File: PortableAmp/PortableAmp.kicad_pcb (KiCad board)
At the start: 2 copper layers, 5 x 45 mm, 19 parts, among them J1 Conn_01x04_Male, J2 Speaker, Q1 MPF102, U1 LM386

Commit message: Minor changes
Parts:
- moved J2 29.8 mm to (144.8, 79.0), turned to 270 degrees
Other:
- board text added: "+"
- board text added: "-"
- board text added: "Speaker"
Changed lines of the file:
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@@
   (general
     (thickness 1.6)
-    (drawings 7)
+    (drawings 10)
     (tracks 0)
     (zones 0)
@@
   )
   (module Connector_PinSocket_2.54mm:PinSocket_1x02_P2.54mm_Vertical (layer F.Cu)
-    (at 149.459001 49.577001)
+    (at 144.78 79 270)
     (descr "Through hole straight socket strip, 1x02, 2.54mm pitch, single row (from Kicad 4.0.7), script generated")
     (tags "Through hole socket strip THT 1x02 2.54mm single row")
-    (fp_text reference J2 (at 0 -2.77) (layer F.SilkS)
-      (effects (font (size 1 1) (thickness 0.15)))
-    )
-    (fp_text value Speaker (at 0 5.31) (layer F.Fab)
+    (fp_text reference J2 (at 0 -2.77 180) (layer F.SilkS)
+      (effects (font (size 1 1) (thickness 0.15)))
+    )
+    (fp_text value Speaker (at 0 5.31 90) (layer F.Fab)
       (effects (font (size 1 1) (thickness 0.15)))
     )
@@
     (fp_line (start 1.75 4.3) (end -1.8 4.3) (layer F.CrtYd) (width 0.05))
     (fp_line (start -1.8 4.3) (end -1.8 -1.8) (layer F.CrtYd) (width 0.05))
-    (fp_text user %R (at 0 1.27 90) (layer F.Fab)
-      (effects (font (size 1 1) (thickness 0.15)))
-    )
-    (pad 1 thru_hole rect (at 0 0) (size 1.7 1.7) (drill 1) (layers *.Cu *.Mask)
-      (net 2 GND))
-    (pad 2 thru_hole oval (at 0 2.54) (size 1.7 1.7) (drill 1) (layers *.Cu *.Mask)
+    (fp_text user %R (at 0 1.27) (layer F.Fab)
+      (effects (font (size 1 1) (thickness 0.15)))
+    )
+    (pad 1 thru_hole rect (at 0 0 270) (size 1.7 1.7) (drill 1) (layers *.Cu *.Mask)
+      (net 2 GND))
+    (pad 2 thru_hole oval (at 0 2.54 270) (size 1.7 1.7) (drill 1) (layers *.Cu *.Mask)
       (net 7 "Net-(C5-Pad2)"))
     (model ${KISYS3DMOD}/Connector_PinSocket_2.54mm.3dshapes/PinSocket_1x02_P2.54mm_Vertical.wrl
@@
       (net 2 GND))
   )
+  (gr_text - (at 144.78 76.23) (layer F.SilkS)
+    (effects (font (size 1.5 1.5) (thickness 0.3)))
+  )
+  (gr_text + (at 142.24 76.23) (layer F.SilkS)
+    (effects (font (size 1.5 1.5) (thickness 0.3)))
+  )
+  (gr_text Speaker (at 143.51 81.77) (layer F.SilkS)
+    (effects (font (size 1 1) (thickness 0.15)))
+  )
   (gr_text GND (at 155.194 93.98) (layer F.SilkS)

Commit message: Finalized board and exported gerbers
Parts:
- moved D1 70.5 mm to (142.2, 107.2)
- moved C4 52.6 mm to (113.3, 94.5), turned to 180 degrees
- moved R2 50.7 mm to (103.6, 98.6)
- moved R1 50.1 mm to (113.8, 102.1), turned to 180 degrees
- moved R3 49.6 mm to (113.8, 105.7), turned to 180 degrees
- moved Q1 43.4 mm to (133.6, 104.6), turned to 180 degrees
- moved C3 43.0 mm to (145.8, 99.8), turned to 180 degrees
- moved H2 42.1 mm to (103.0, 115.0)
- moved U1 40.1 mm to (128.5, 91.9)
- moved H1 38.5 mm to (103.0, 80.0)
- moved C1 34.4 mm to (122.4, 93.5), turned to 180 degrees
- moved C2 32.5 mm to (113.3, 85.2), turned to 180 degrees
- moved C5 29.2 mm to (145.8, 90.4), turned to 180 degrees
- moved RV1 27.8 mm to (117.9, 80.3), turned to 270 degrees
- moved RV2 17.0 mm to (129.5, 80.3), turned to 270 degrees
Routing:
- net Input: track 0.00 -> 53.7 mm
- net Net-(C2-Pad1): track 0.00 -> 46.4 mm
- net Net-(C5-Pad1): track 0.00 -> 44.3 mm
- net Net-(C1-Pad1): track 0.00 -> 33.5 mm
- net Net-(RV2-Pad2): track 0.00 -> 25.4 mm
- net Net-(C4-Pad1): track 0.00 -> 14.8 mm
- net Net-(RV2-Pad1): track 0.00 -> 14.4 mm
- net Net-(RV1-Pad2): track 0.00 -> 12.5 mm
- net Net-(C5-Pad2): track 0.00 -> 12.4 mm
- net Net-(C2-Pad2): track 0.00 -> 11.7 mm
- net Net-(C3-Pad2): track 0.00 -> 7.66 mm
- net 9V: track 0.00 -> 5.75 mm
- added copper zone on B.Cu, net GND
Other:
- board size 5 x 45 mm -> 59 x 45 mm
- board text added: "Gain"
- board text added: "JLCJLCJLCJLC"
- board text added: "Thomas McDonagh Portable Amp V1.0 mcdonaghcorp.com"
- board text added: "Volume"

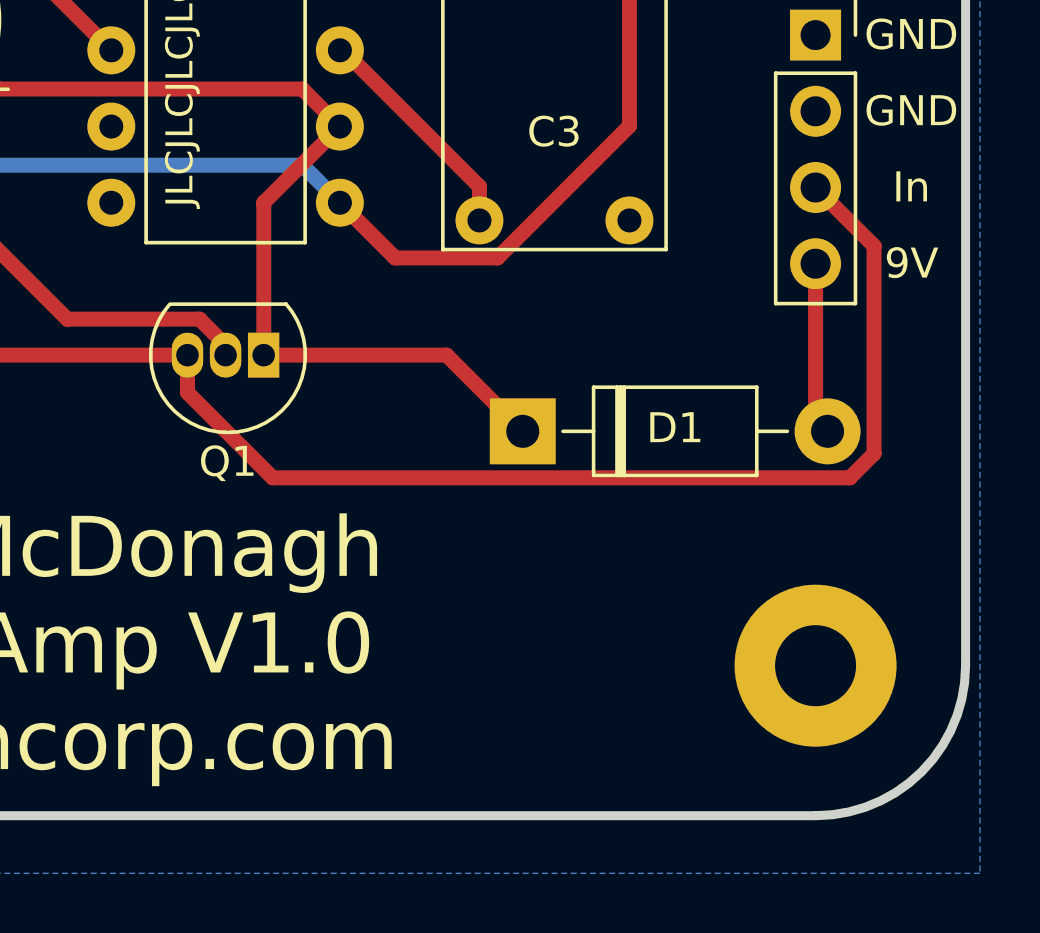
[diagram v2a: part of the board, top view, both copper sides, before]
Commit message: Added power switch pins and replotted gerber files
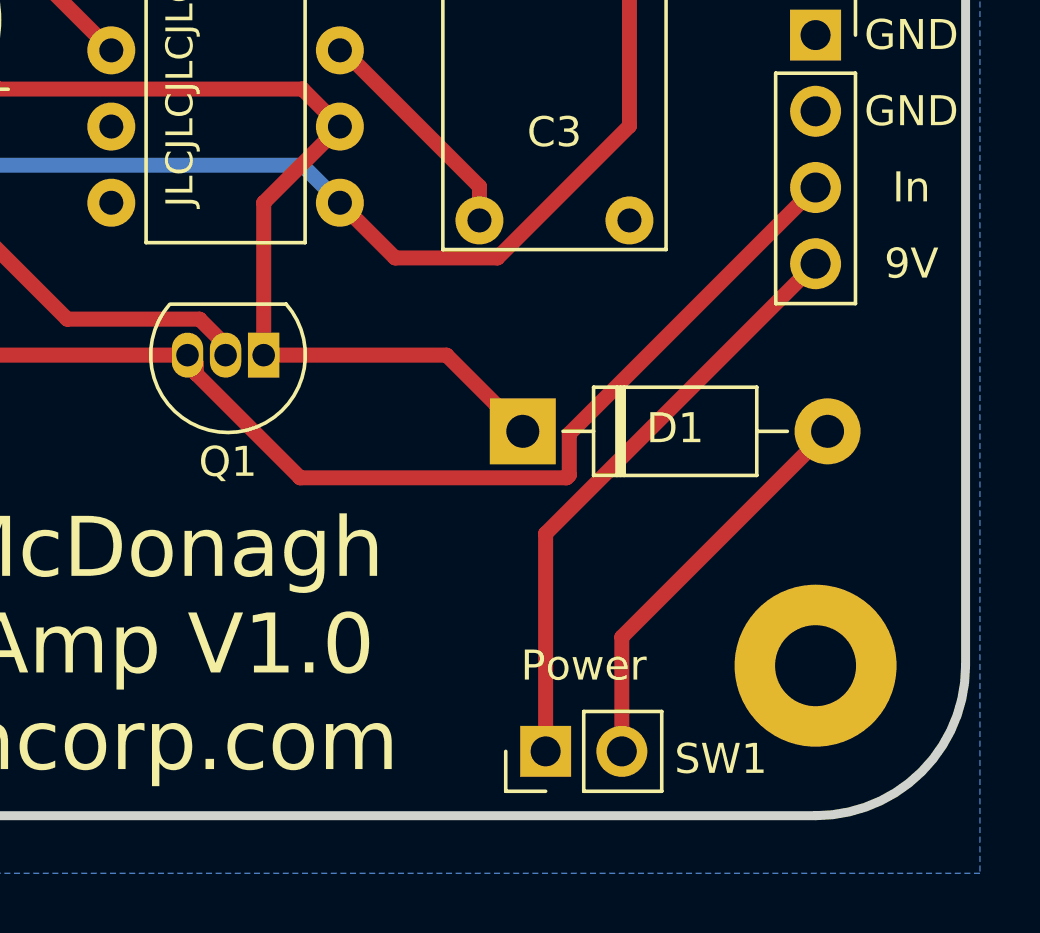
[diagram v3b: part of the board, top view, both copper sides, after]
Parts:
- added SW1: Power, Connector_PinHeader_2.54mm:PinHeader_1x02_P2.54mm_Vertical, F.Cu at (143.0, 117.9)
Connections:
- D1 pad 2: 9V -> Net-(D1-Pad2)
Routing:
- net 9V: track 5.75 -> 20.0 mm
- net Net-(D1-Pad2): track 0.00 -> 13.5 mm
- net Input: track 53.7 -> 46.0 mm
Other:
- board text added: "Power"

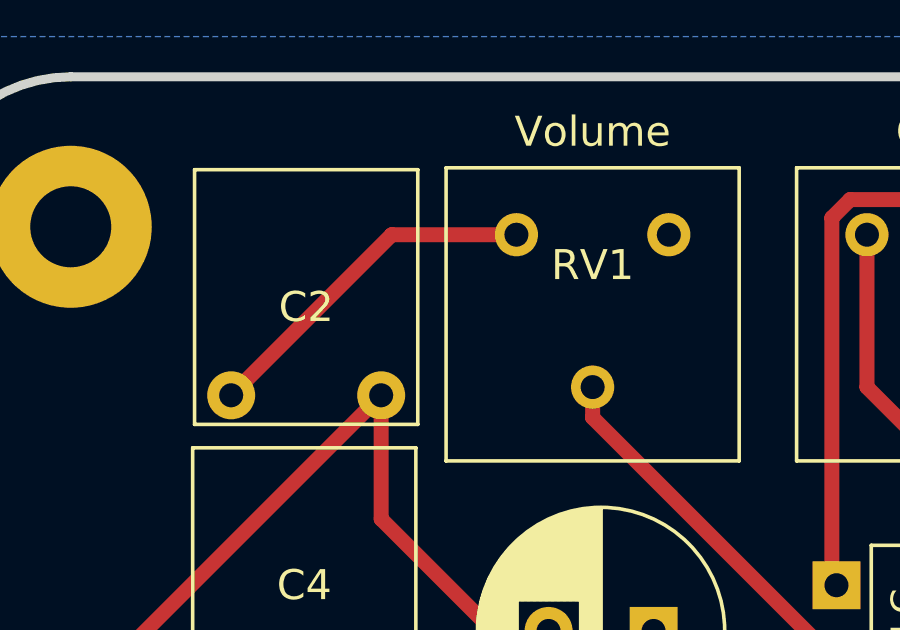
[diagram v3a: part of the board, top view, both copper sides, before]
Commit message: Flipped potentiometer to make more sense. Replotted Gerber files
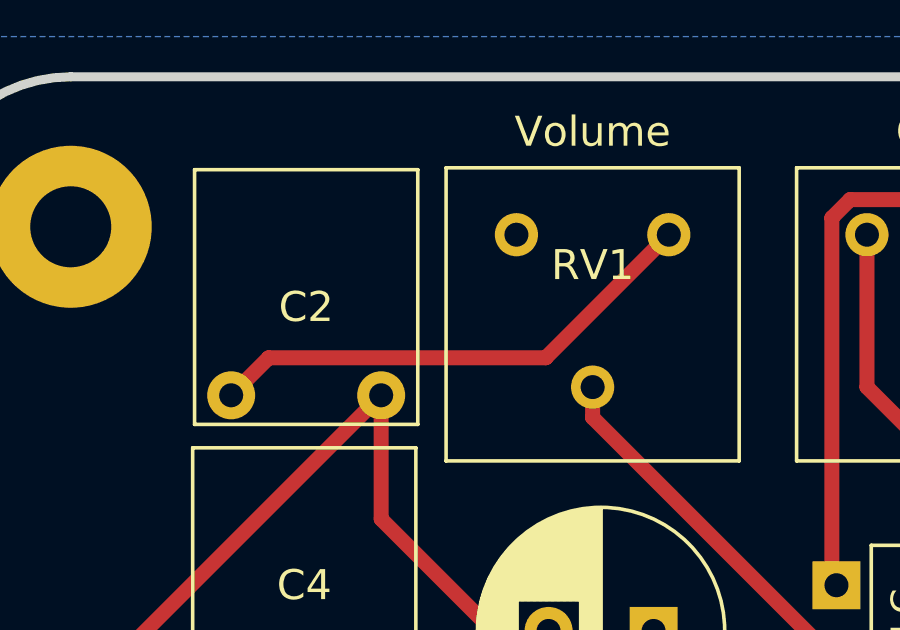
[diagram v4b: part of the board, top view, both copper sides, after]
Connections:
- RV1 pad 1: Net-(C2-Pad2) -> GND
- RV1 pad 3: GND -> Net-(C2-Pad2)
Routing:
- net Net-(C2-Pad2): track 11.7 -> 16.8 mm

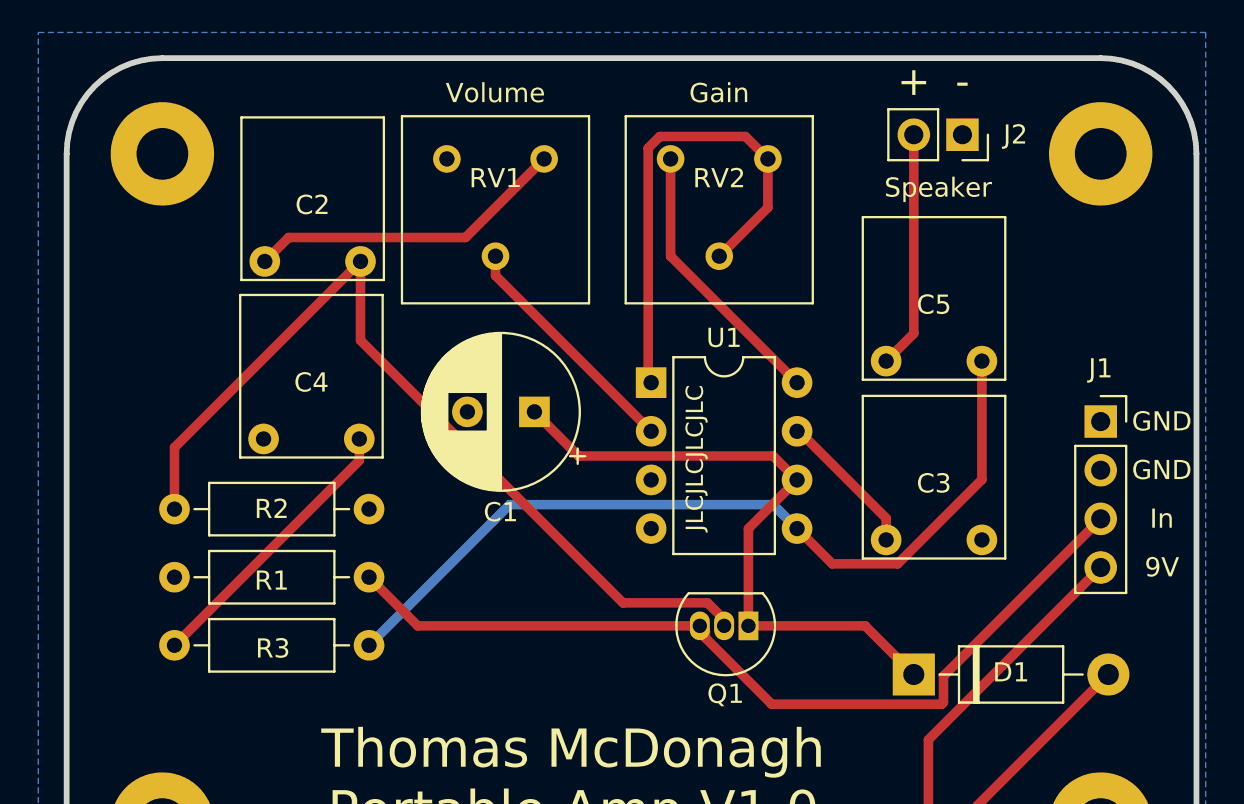
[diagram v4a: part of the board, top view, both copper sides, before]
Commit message: Realized I need higher voltage tolerant capacitors. Still need to pick better ones.
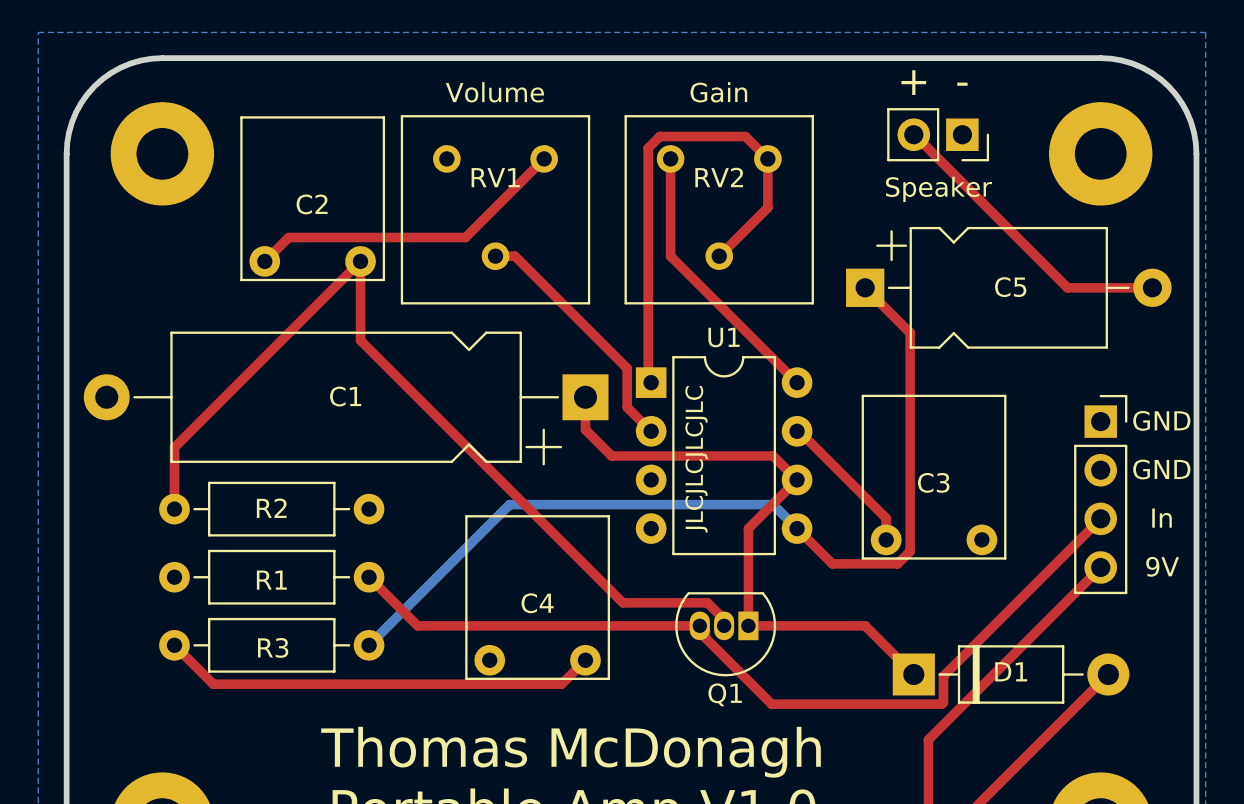
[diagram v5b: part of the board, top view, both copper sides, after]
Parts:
- C1: footprint Capacitor_THT:CP_Radial_D8.0mm_P3.50mm -> Capacitor_THT:CP_Axial_L18.0mm_D6.5mm_P25.00mm_Horizontal
- C5: footprint libraries:C_Flat_L7.2_H6.5 -> Capacitor_THT:CP_Axial_L10.0mm_D6.0mm_P15.00mm_Horizontal
- moved C4 16.5 mm to (125.1, 106.0)
- moved C5 6.99 mm to (139.7, 87.0), turned to 0 degrees
- moved C1 2.77 mm to (125.1, 92.7)
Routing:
- net Net-(C4-Pad1): track 14.8 -> 22.8 mm
- net Net-(C5-Pad2): track 12.4 -> 15.8 mm
- net Net-(C5-Pad1): track 44.3 -> 47.6 mm
- net Net-(C1-Pad1): track 33.5 -> 32.2 mm
- net Net-(RV1-Pad2): track 12.5 -> 13.1 mm
